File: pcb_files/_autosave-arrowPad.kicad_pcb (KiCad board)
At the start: 2 copper layers, 102.9 x 83.8 mm, 43 parts, among them J1 AudioJack3_Ground, J2 AudioJack3_Ground, K1 KEYSW, K10 KEYSW, K11 KEYSW, K12 KEYSW, K13 KEYSW, K14 KEYSW, K15 KEYSW, K16 KEYSW, K2 KEYSW, K3 KEYSW, K4 KEYSW, K5 KEYSW, K6 KEYSW, K7 KEYSW, K8 KEYSW, K9 KEYSW, U1 ProMicro, U2 NRF24L01_Breakout, U3 ADG417BN, U4 AMS1117-3.3, U5 ADG417BN, U6 ADG417BN

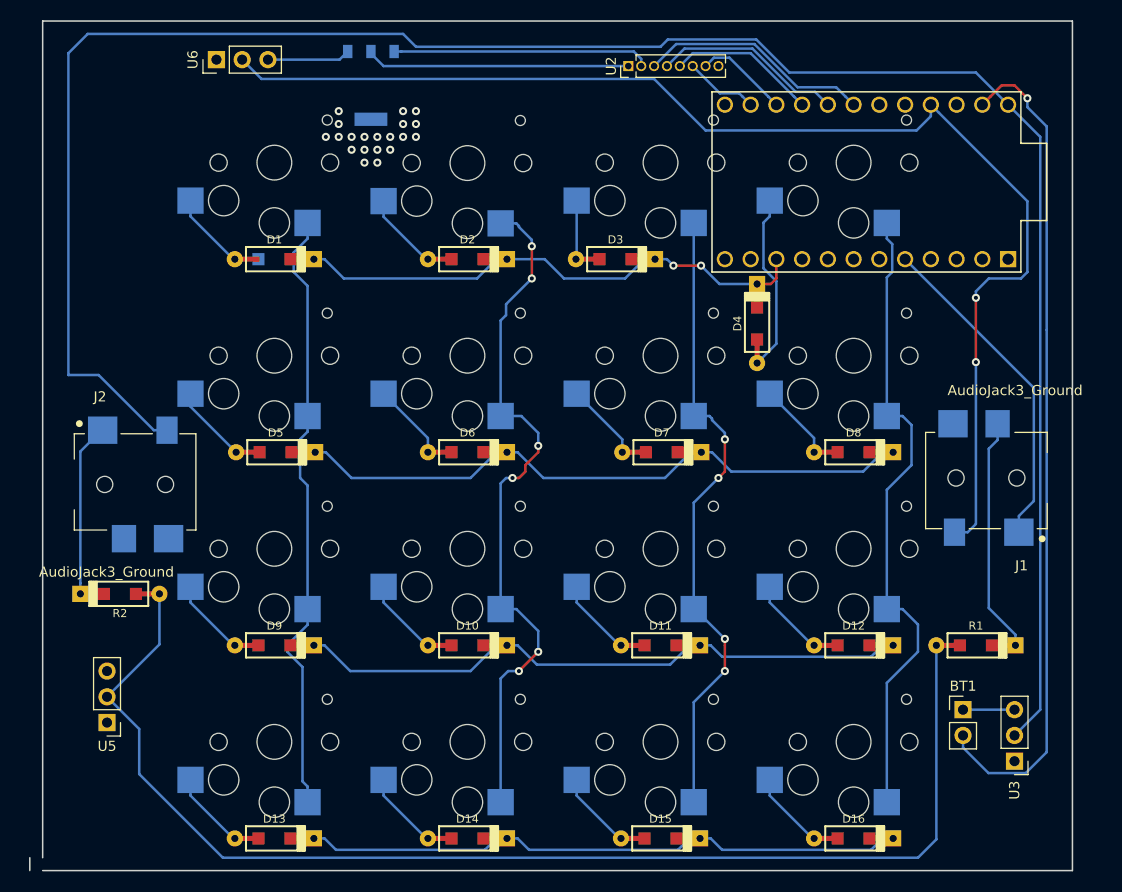
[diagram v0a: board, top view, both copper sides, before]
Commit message: TLC5940 LED controller
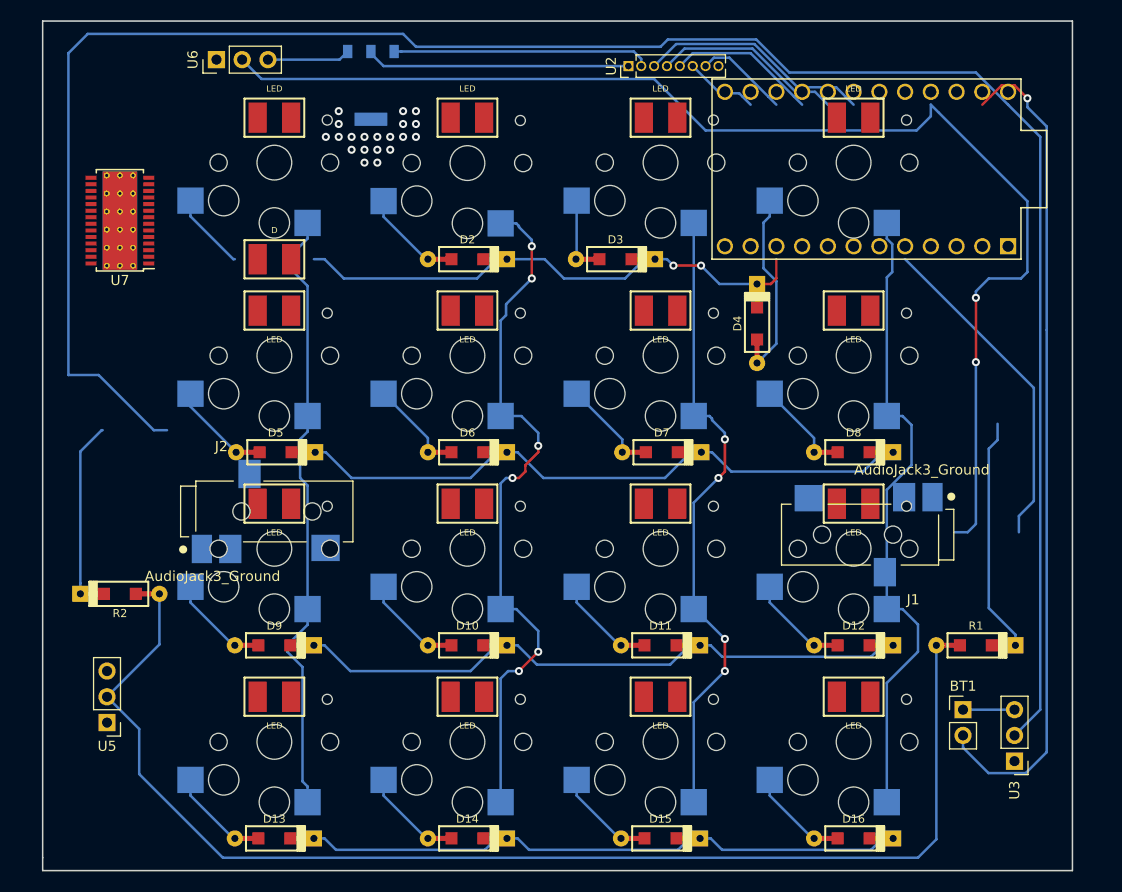
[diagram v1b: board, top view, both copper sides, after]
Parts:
- added D20: LED, keyboard_parts:C_3528, F.Cu at (130.8, 60.3)
- added D21: LED, keyboard_parts:C_3528, F.Cu at (149.9, 60.3)
- added D22: LED, keyboard_parts:C_3528, F.Cu at (168.9, 60.3)
- added D23: LED, keyboard_parts:C_3528, F.Cu at (188.0, 60.3)
- added D24: LED, keyboard_parts:C_3528, F.Cu at (130.8, 79.4)
- added D25: LED, keyboard_parts:C_3528, F.Cu at (149.9, 79.4)
- added D26: LED, keyboard_parts:C_3528, F.Cu at (168.9, 79.4)
- added D27: LED, keyboard_parts:C_3528, F.Cu at (188.0, 79.4)
- added D28: LED, keyboard_parts:C_3528, F.Cu at (130.8, 98.4)
- added D29: LED, keyboard_parts:C_3528, F.Cu at (149.9, 98.4)
- added D30: LED, keyboard_parts:C_3528, F.Cu at (168.9, 98.4)
- added D31: LED, keyboard_parts:C_3528, F.Cu at (188.0, 98.4)
- added D32: LED, keyboard_parts:C_3528, F.Cu at (130.8, 117.5)
- added D33: LED, keyboard_parts:C_3528, F.Cu at (149.9, 117.5)
- added D34: LED, keyboard_parts:C_3528, F.Cu at (168.9, 117.5)
- added D35: LED, keyboard_parts:C_3528, F.Cu at (188.0, 117.5)
- added U7: TLC5940PWP, Package_SO:HTSSOP-28-1EP_4.4x9.7mm_P0.65mm_EP3.4x9.5mm_Mask2.4x6.17mm_ThermalVias, F.Cu at (115.6, 70.5)
- D1: footprint keyboard_parts:D_SOD123_axial -> keyboard_parts:C_3528
- J1, J2: footprint foots:CUI_SJ1-3514-SMT[PAD1,2,34]Backside -> foots:CUI_SJ-43514-SMT(1,2,3,4reverseside)
- moved J2 15.5 mm to (130.8, 99.2)
- moved J1 15.0 mm to (188.6, 101.5)
- moved U1 1.27 mm to (189.2, 65.4)
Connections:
- U1 pad 1: Net-(U1-Pad1) -> /Col2
- U1 pad 13: /Row3 -> Net-(U1-Pad13)
- U1 pad 2: Net-(U1-Pad2) -> /Row3
- U1 pad 8: /Col2 -> /GSCLK
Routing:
- net Net-(J1-Pad1): track 49.9 -> 17.1 mm
- net /VCC1: track 124.3 -> 157.1 mm
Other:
- board size 102.9 x 83.8 mm -> 101.6 x 83.8 mm
